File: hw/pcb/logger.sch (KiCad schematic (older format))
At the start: 54 parts, among them J1 BAT+, J2 SWO, J3 DEBUG, J4 USB_B_Micro, J5 ANT1575-2006B, J6 OLED-128O064D, J7 BAT-, SW1 Next, SW2 Select, U1 STM32F070CBT6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

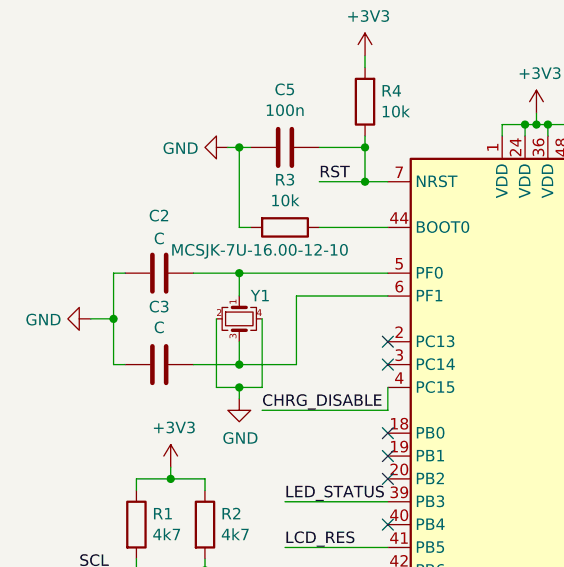
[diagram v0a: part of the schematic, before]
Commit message: Added value to crystal caps
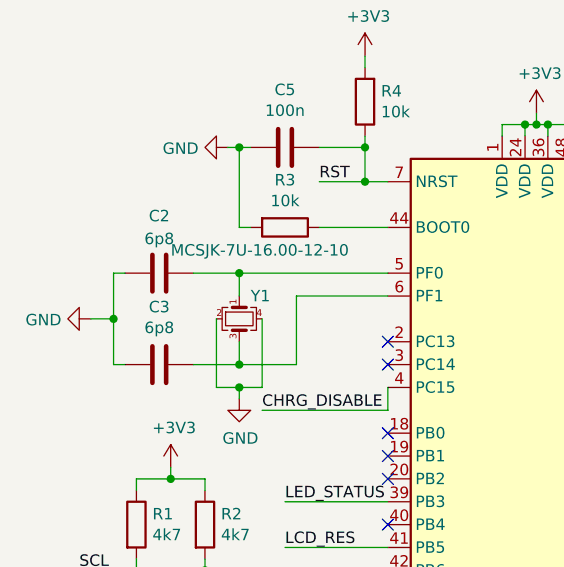
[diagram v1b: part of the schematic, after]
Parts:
- C2, C3: value C -> 6p8
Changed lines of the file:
@@
 P 1100 4000
 F 0 "C2" V 850 4000 50  0000 C CNN
-F 1 "C" V 950 4000 50  0000 C CNN
+F 1 "6p8" V 950 4000 50  0000 C CNN
 F 2 "Capacitor_SMD:C_0603_1608Metric" H 1138 3850 50  0001 C CNN
 F 3 "~" H 1100 4000 50  0001 C CNN
@@
 P 1100 4400
 F 0 "C3" V 848 4400 50  0000 C CNN
-F 1 "C" V 939 4400 50  0000 C CNN
+F 1 "6p8" V 939 4400 50  0000 C CNN
 F 2 "Capacitor_SMD:C_0603_1608Metric" H 1138 4250 50  0001 C CNN
 F 3 "~" H 1100 4400 50  0001 C CNN
